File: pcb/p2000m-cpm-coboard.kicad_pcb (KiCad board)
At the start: 2 copper layers, 0 parts

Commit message: Adding Python script to analyze wiring and add TODO with current fixes to make
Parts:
- added C1: 0.1uF, Capacitor_THT:C_Disc_D5.0mm_W2.5mm_P5.00mm, F.Cu at (135.3, 94.6)
- added C2: 0.1uF, Capacitor_THT:C_Disc_D5.0mm_W2.5mm_P5.00mm, F.Cu at (135.3, 98.7)
- added C3: 0.1uF, Capacitor_THT:C_Disc_D5.0mm_W2.5mm_P5.00mm, F.Cu at (135.3, 102.7)
- added C4: 0.1uF, Capacitor_THT:C_Disc_D5.0mm_W2.5mm_P5.00mm, F.Cu at (135.3, 106.8)
- added C5: 0.1uF, Capacitor_THT:C_Disc_D5.0mm_W2.5mm_P5.00mm, F.Cu at (135.3, 110.8)
- added C6: 0.1uF, Capacitor_THT:C_Disc_D5.0mm_W2.5mm_P5.00mm, F.Cu at (135.3, 114.9)
- added C7: 100uF, Capacitor_THT:C_Radial_D6.3mm_H5.0mm_P2.50mm, F.Cu at (126.3, 133.8)
- added J1: CPU BOARD, Connector_PinHeader_2.54mm:PinHeader_2x20_P2.54mm_Vertical, F.Cu at (83.1, 72.9)
- added J2: EXPANSION BOARD, Connector_PinHeader_2.54mm:PinHeader_2x20_P2.54mm_Vertical, F.Cu at (90.2, 72.9)
- added J3: T/~{M}, Connector_PinHeader_2.54mm:PinHeader_1x03_P2.54mm_Vertical, F.Cu at (144.2, 72.9)
- added J4: POWER, Connector_PinHeader_2.54mm:PinHeader_1x02_P2.54mm_Vertical, F.Cu at (116.7, 132.2)
- added J5: POWER, Connector_PinHeader_2.54mm:PinHeader_1x02_P2.54mm_Vertical, F.Cu at (121.3, 132.2)
- added R1: 2k2, Resistor_THT:R_Axial_DIN0207_L6.3mm_D2.5mm_P7.62mm_Horizontal, F.Cu at (82.4, 125.5)
- added R2: 2k2, Resistor_THT:R_Axial_DIN0207_L6.3mm_D2.5mm_P7.62mm_Horizontal, F.Cu at (82.4, 129.6)
- added U1: CY62256-70PC, Package_DIP:DIP-28_W15.24mm_Socket, F.Cu at (116.5, 94.7)
- added U2: SST39SF010, Package_DIP:DIP-32_W15.24mm_Socket, F.Cu at (97.1, 94.7)
- added U3: DIL16, Package_DIP:DIP-16_W7.62mm_Socket, F.Cu at (97.1, 72.7)
- added U4: 74LS74, Package_DIP:DIP-14_W7.62mm_Socket, F.Cu at (135.8, 119.0)
- added U5: 74LS138, Package_DIP:DIP-16_W7.62mm_Socket, F.Cu at (108.8, 72.7)
- added U6: 74LS283, Package_DIP:DIP-16_W7.62mm_Socket, F.Cu at (120.5, 72.7)
- added U7: 82S123, Package_DIP:DIP-16_W7.62mm_Socket, F.Cu at (132.2, 72.7)

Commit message: Initial commit of PCB layout and fixing some bugs
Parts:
- J1, J2: footprint Connector_PinHeader_2.54mm:PinHeader_2x20_P2.54mm_Vertical -> Connector_IDC:IDC-Header_2x20_P2.54mm_Vertical
- J5: value POWER -> TERMINAL; footprint Connector_PinHeader_2.54mm:PinHeader_1x02_P2.54mm_Vertical -> TerminalBlock_RND:TerminalBlock_RND_205-00232_1x02_P5.08mm_Horizontal
- moved J5 94.3 mm to (148.5, 41.9), turned to -90 degrees
- moved C5 92.3 mm to (71.1, 44.5), turned to -90 degrees
- moved J4 88.8 mm to (137.2, 45.7), turned to 180 degrees
- moved C6 86.3 mm to (71.1, 57.2), turned to -90 degrees
- moved C7 73.8 mm to (148.6, 63.5)
- moved C4 71.9 mm to (73.7, 69.9), turned to -90 degrees
- moved U4 71.3 mm to (78.7, 76.2), turned to 90 degrees
- moved C3 67.3 mm to (71.1, 82.6), turned to -90 degrees
- moved U7 58.3 mm to (76.2, 88.9), turned to 90 degrees
- moved J2 57.8 mm to (40.6, 43.2)
- moved U6 49.5 mm to (76.2, 50.8), turned to 90 degrees
- moved C1 45.9 mm to (104.1, 61.0), turned to -90 degrees
- moved J1 38.6 mm to (58.4, 43.2)
- moved R2 36.1 mm to (76.2, 94.0)
- moved C2 35.7 mm to (104.1, 81.3), turned to -90 degrees
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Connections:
- net RAMS3 renamed ~{RAMS3}
- J5 pad 1: VCC -> GND
- J5 pad 2: GND -> VCC
- U2 pad 6: GND -> ~{MRQ}
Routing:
- net GND: track 0.00 -> 745.4 mm, vias 0 -> 4
- net VCC: track 0.00 -> 401.9 mm
- net ~{WR}: track 0.00 -> 18.8 mm
- net D5: track 0.00 -> 18.8 mm
- net D3: track 0.00 -> 18.8 mm
- net D1: track 0.00 -> 18.8 mm
- net D: track 0.00 -> 18.8 mm
- net ~{WAIT}: track 0.00 -> 18.8 mm
- net ~{RD}: track 0.00 -> 18.8 mm
- net ~{PHI}: track 0.00 -> 18.8 mm
- net D7: track 0.00 -> 18.8 mm
- net A9: track 0.00 -> 18.8 mm
- net A7: track 0.00 -> 18.8 mm
- net A5: track 0.00 -> 18.8 mm
- net A3: track 0.00 -> 18.8 mm
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- added copper zone on F.Cu, net GND
- added copper zone on B.Cu, net VCC
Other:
- board outline added: 122.9 x 63.5 mm
- board text added: "1"
- board text added: "2"
- board text added: "39"
- board text added: "40"
- board text added: "Connect to CPU board via 16-pin ribbon cable"
- board text added: "Connect to CPU board via 40-pin ribbon cable"
- board text added: "Connect to expansion board via 40-pin ribbon cable"
- board text added: "Insert PROM from CPU board"
- board text added: "P2000T/M CP/M Coboard"
- board text added: "https://github.com/ifilot/p2000m-cpm-coboard"
- board text added: "v1"

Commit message: Polishing PCB
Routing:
- net A0: track 18.7 -> 182.7 mm, vias 0 -> 1
- net A12: track 0.00 -> 163.9 mm, vias 0 -> 3
- net A14: track 0.00 -> 163.1 mm, vias 0 -> 2
- net A13: track 0.00 -> 157.2 mm, vias 0 -> 1
- net A11: track 18.8 -> 163.7 mm
- net P7: track 0.00 -> 130.1 mm
- net A15: track 0.00 -> 124.8 mm, vias 0 -> 2
- net D0: track 18.7 -> 140.2 mm
- net A10: track 18.7 -> 137.9 mm, vias 0 -> 2
- net D1: track 18.8 -> 133.5 mm
- net P2: track 0.00 -> 112.5 mm, vias 0 -> 2
- net P0: track 0.00 -> 110.1 mm, vias 0 -> 2
- net P1: track 0.00 -> 108.2 mm, vias 0 -> 1
- net ~{RD}: track 18.8 -> 120.7 mm, vias 0 -> 3
- net D2: track 18.7 -> 118.8 mm, vias 0 -> 1
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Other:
- board text added: "M"
- board text added: "T"

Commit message: Adding pull-up resistor to RAMS3/ and updating mappings
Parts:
- added R3: 4k7, Resistor_THT:R_Axial_DIN0207_L6.3mm_D2.5mm_P7.62mm_Horizontal, F.Cu at (149.5, 54.7)
- moved C7 6.01 mm to (148.2, 69.5)
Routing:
- net ~{RAMS3}: track 41.9 -> 65.1 mm
- net VCC: track 420.7 -> 423.7 mm
- net GND: track 774.8 -> 775.6 mm

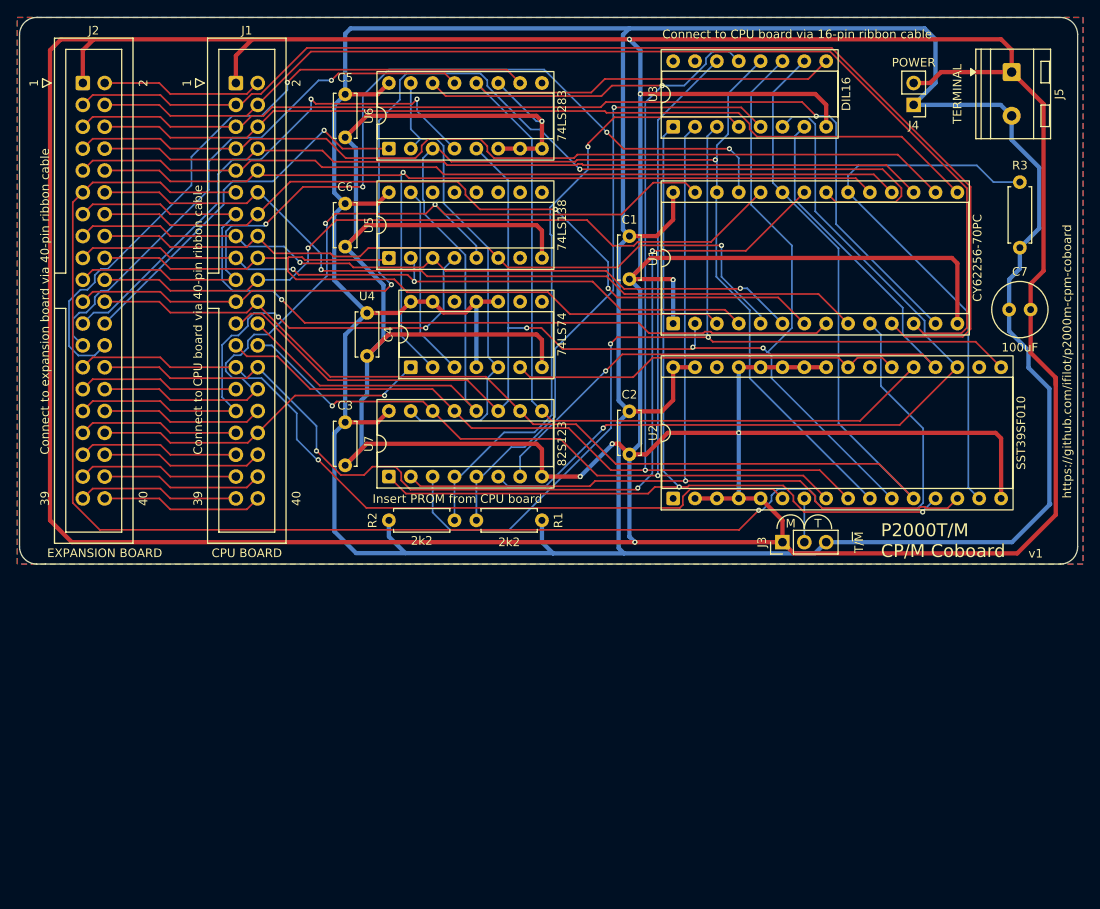
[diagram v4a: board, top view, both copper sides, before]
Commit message: Replacing DIP for PLCC32 for SST39SF010
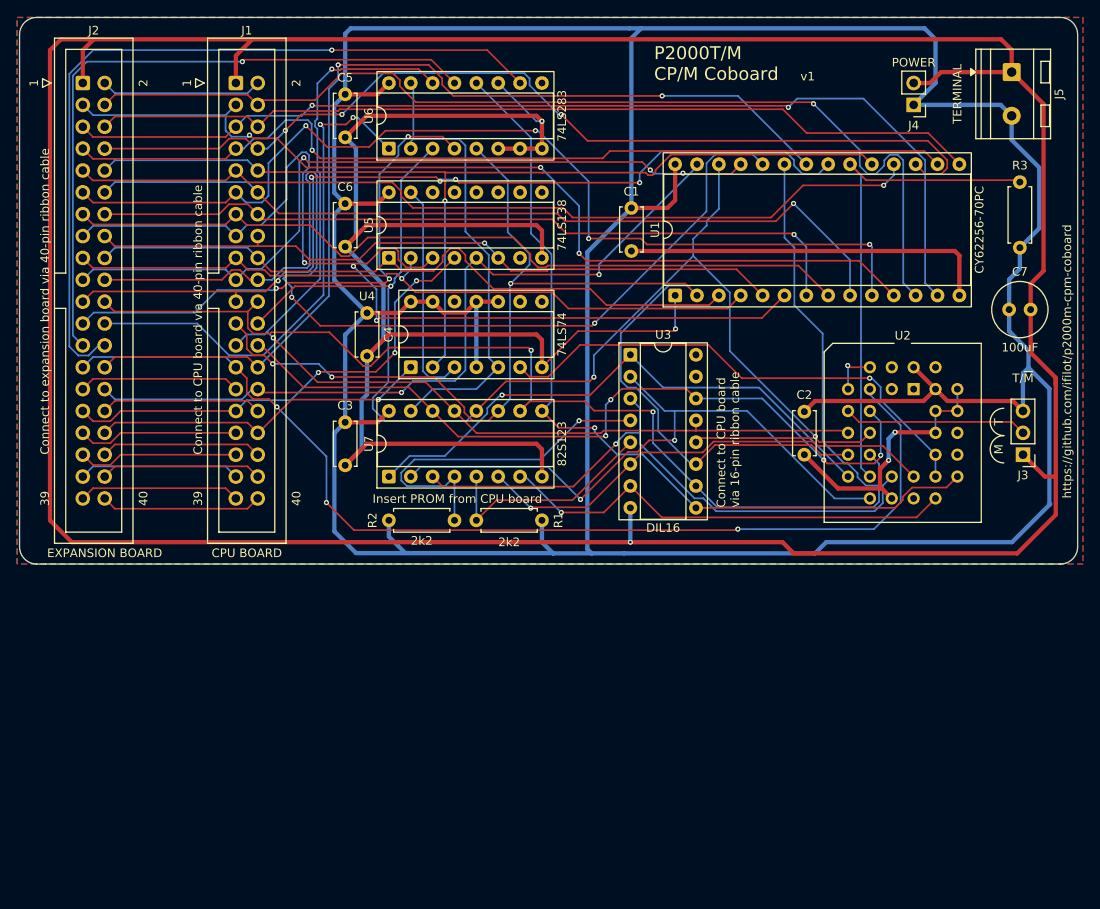
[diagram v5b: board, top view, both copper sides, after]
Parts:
- U2: footprint Package_DIP:DIP-32_W15.24mm_Socket -> Package_LCC:PLCC-32_THT-Socket
- moved U2 30.7 mm to (137.2, 78.7), turned to 0 degrees
- moved J3 29.7 mm to (149.9, 86.4), turned to 180 degrees
- moved U3 27.0 mm to (104.2, 74.8), turned to 0 degrees
- moved C2 20.3 mm to (124.5, 81.4)
- moved U1 3.27 mm to (109.5, 67.9)
- moved C1 3.27 mm to (104.4, 57.7)
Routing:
- net GND: track 775.6 -> 641.1 mm, vias 8 -> 6
- net A0: track 182.7 -> 116.0 mm, vias 1 -> 4
- net P4: track 74.1 -> 26.7 mm, vias 1 -> 0
- net P0: track 110.1 -> 65.4 mm, vias 2 -> 1
- net P5: track 99.3 -> 54.7 mm
- net P2: track 112.5 -> 68.3 mm, vias 2 -> 1
- net A9: track 84.8 -> 123.4 mm, vias 1 -> 2
- net A14: track 163.1 -> 124.7 mm
- net P6: track 91.3 -> 53.7 mm
- net P1: track 108.2 -> 72.6 mm, vias 1 -> 2
- net A15: track 124.8 -> 90.9 mm, vias 2 -> 4
- net A10: track 137.9 -> 104.8 mm, vias 2 -> 5
- net A4: track 87.4 -> 120.4 mm, vias 2 -> 3
- net P7: track 130.1 -> 97.1 mm, vias 0 -> 1
- net ~{MRQ}: track 92.7 -> 123.9 mm, vias 1 -> 3
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
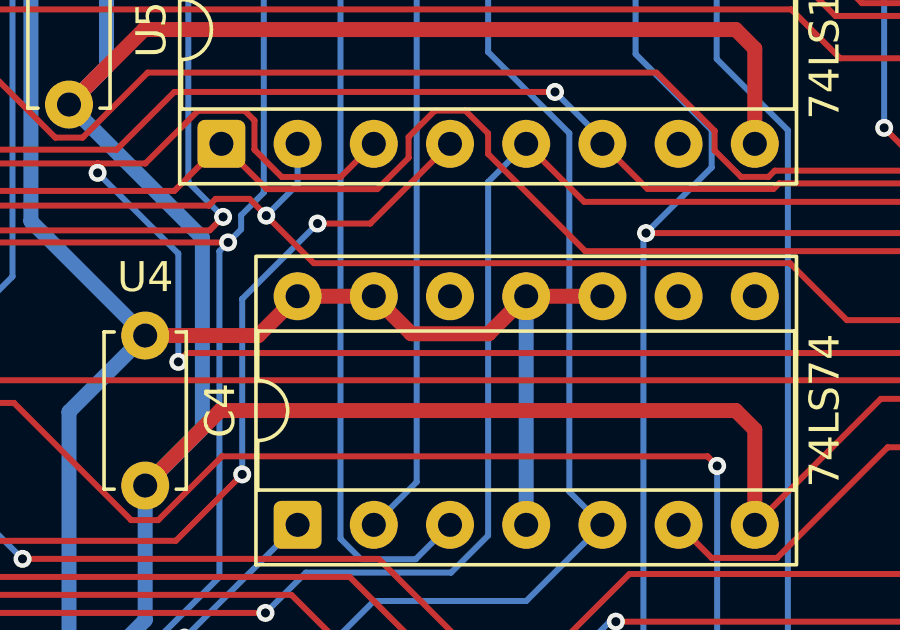
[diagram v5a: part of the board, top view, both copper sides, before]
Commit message: Adding 82S123 contents
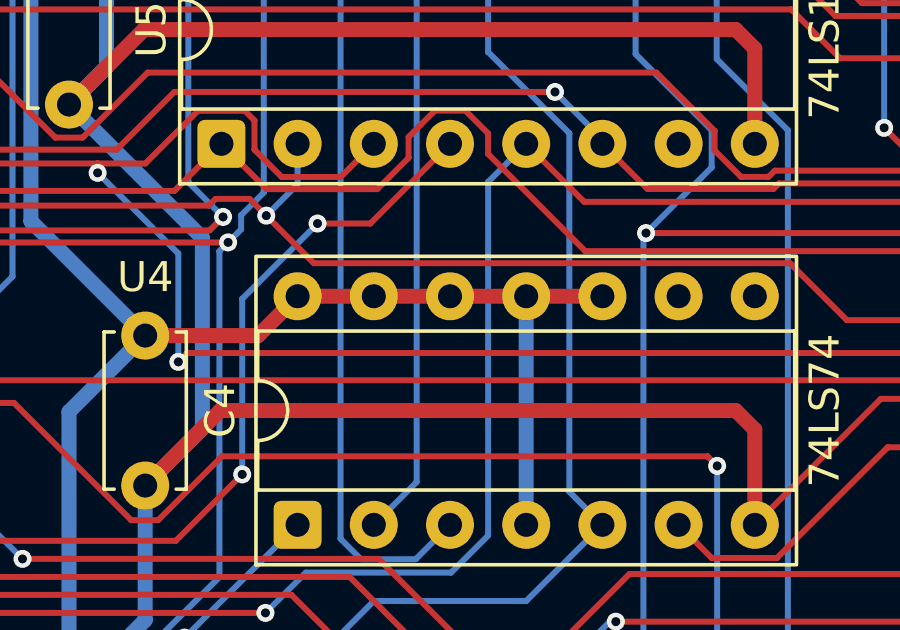
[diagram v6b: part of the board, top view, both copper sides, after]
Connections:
- U4 pad 12: unconnected-(U4B-D-Pad12) -> VCC
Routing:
- net VCC: track 449.1 -> 448.0 mm

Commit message: Rerouting by hand
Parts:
- added C8: 0.1uF, Capacitor_THT:C_Disc_D5.0mm_W2.5mm_P5.00mm, F.Cu at (73.7, 82.6)
- added U8: 74LS02, Package_DIP:DIP-14_W7.62mm_Socket, F.Cu at (78.7, 88.9)
- C7: footprint Capacitor_THT:C_Radial_D6.3mm_H5.0mm_P2.50mm -> Capacitor_THT:CP_Radial_D6.3mm_P2.50mm
- moved C3 38.5 mm to (107.9, 71.1), turned to 180 degrees
- moved C7 29.6 mm to (134.7, 43.2)
- moved U7 28.4 mm to (101.6, 76.2), turned to 0 degrees
- moved R1 19.0 mm to (74.9, 94.0), turned to 0 degrees
- moved C2 17.3 mm to (138.3, 71.1), turned to 180 degrees
- moved R2 10.2 mm to (86.4, 94.0)
- moved U3 10.2 mm to (114.3, 76.2)
- moved J4 4.62 mm to (141.6, 44.5)
- moved J5 1.83 mm to (149.9, 40.6)
- moved C1 1.81 mm to (104.4, 55.9)
- moved U1 1.81 mm to (109.5, 66.0)
- moved J3 1.35 mm to (150.8, 87.3)
- moved U2 1.27 mm to (137.2, 80.0)
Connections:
- U1 pad 20: ~{RAMS3} -> Net-(U1-~{CS})
- U2 pad 6: ~{MRQ} -> GND
- U4 pad 3: /OUT_$2x -> Net-(U4A-C)
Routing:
- net VCC: track 448.0 -> 332.0 mm, vias 0 -> 1
- net Net-(U1-~{CS}): track 0.00 -> 79.9 mm, vias 0 -> 4
- net ~{MRQ}: track 123.9 -> 61.6 mm, vias 3 -> 1
- net ~{RAMS3}: track 57.8 -> 113.5 mm, vias 0 -> 2
- net GND: track 641.1 -> 602.7 mm, vias 6 -> 5
- net A9: track 123.4 -> 86.5 mm, vias 2 -> 1
- net RA12: track 62.1 -> 93.0 mm
- net P1: track 72.6 -> 44.0 mm, vias 2 -> 1
- net P0: track 65.4 -> 41.5 mm
- net A5: track 82.3 -> 102.1 mm, vias 1 -> 2
- net RA13: track 59.6 -> 78.3 mm, vias 2 -> 3
- net A6: track 83.5 -> 101.7 mm, vias 1 -> 2
- net A2: track 93.8 -> 111.7 mm, vias 0 -> 1
- net A7: track 79.3 -> 96.7 mm, vias 0 -> 2
- net /~{T_SEL}: track 53.8 -> 71.0 mm, vias 0 -> 2
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- removed copper zone on F.Cu, net GND
- removed copper zone on B.Cu, net VCC
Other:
- board text added: "+"
- board text added: "-"
- board text added: "v1.1"
- board text removed: "v1"

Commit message: Fixing bug in wiring
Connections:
- U8 pad 10: unconnected-(U8-Pad10) -> Net-(U1-~{CS})
- U8 pad 4: Net-(U1-~{CS}) -> Net-(U8-Pad4)
- U8 pad 8: VCC -> Net-(U8-Pad4)
- U8 pad 9: VCC -> Net-(U8-Pad4)
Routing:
- net Net-(U8-Pad4): track 0.00 -> 22.8 mm
- net Net-(U1-~{CS}): track 79.9 -> 68.1 mm, vias 4 -> 3
- net VCC: track 332.0 -> 323.5 mm
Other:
- board text added: "v1.2"
- board text removed: "v1.1"
